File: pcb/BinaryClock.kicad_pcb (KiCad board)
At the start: 2 copper layers, 28.4 x 41.7 mm, 17 parts, among them CON1 AVR-ISP-6, CON2 BARREL_JACK, IC1 ATMEGA328P-A, U1 MC33269, U2 DS3231, U3 clock_header, U4 clock_header, U5 clock_header, Y1 16MHz

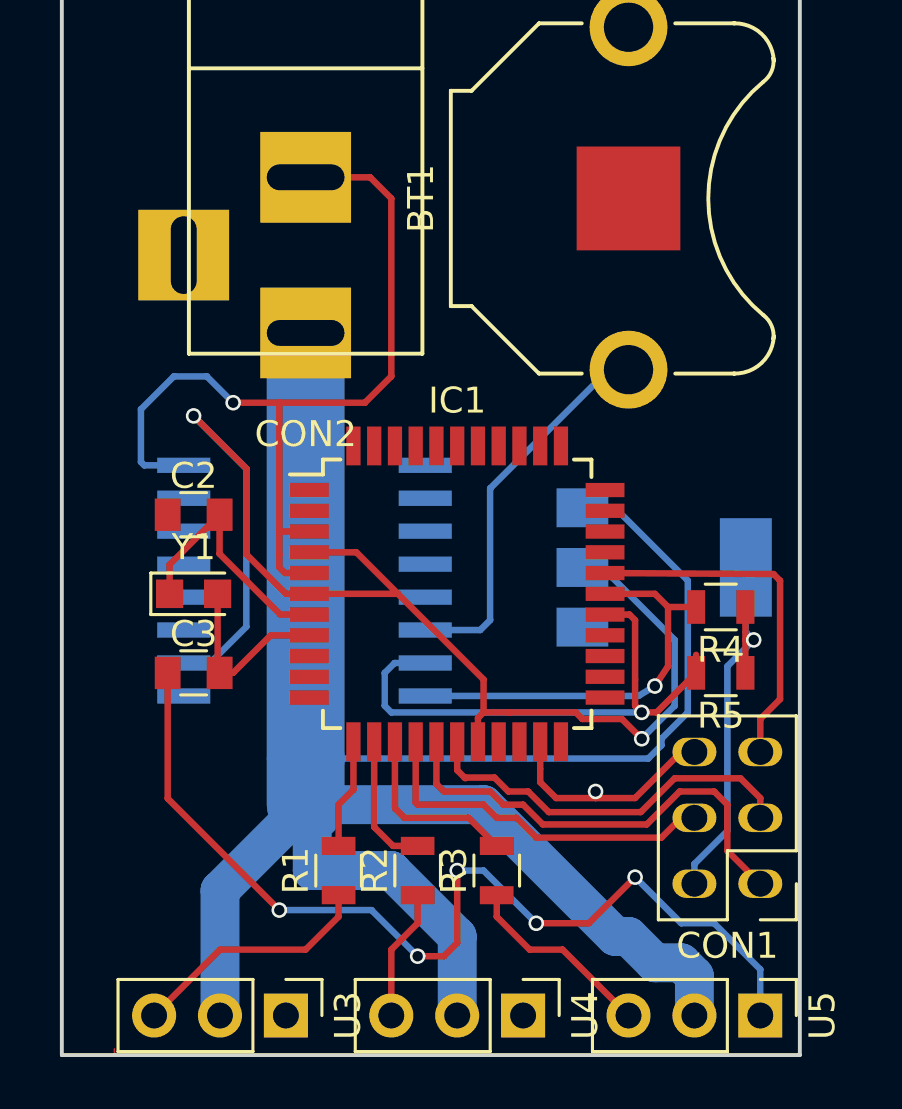
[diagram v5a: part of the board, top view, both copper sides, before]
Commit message: Added silkscreen text
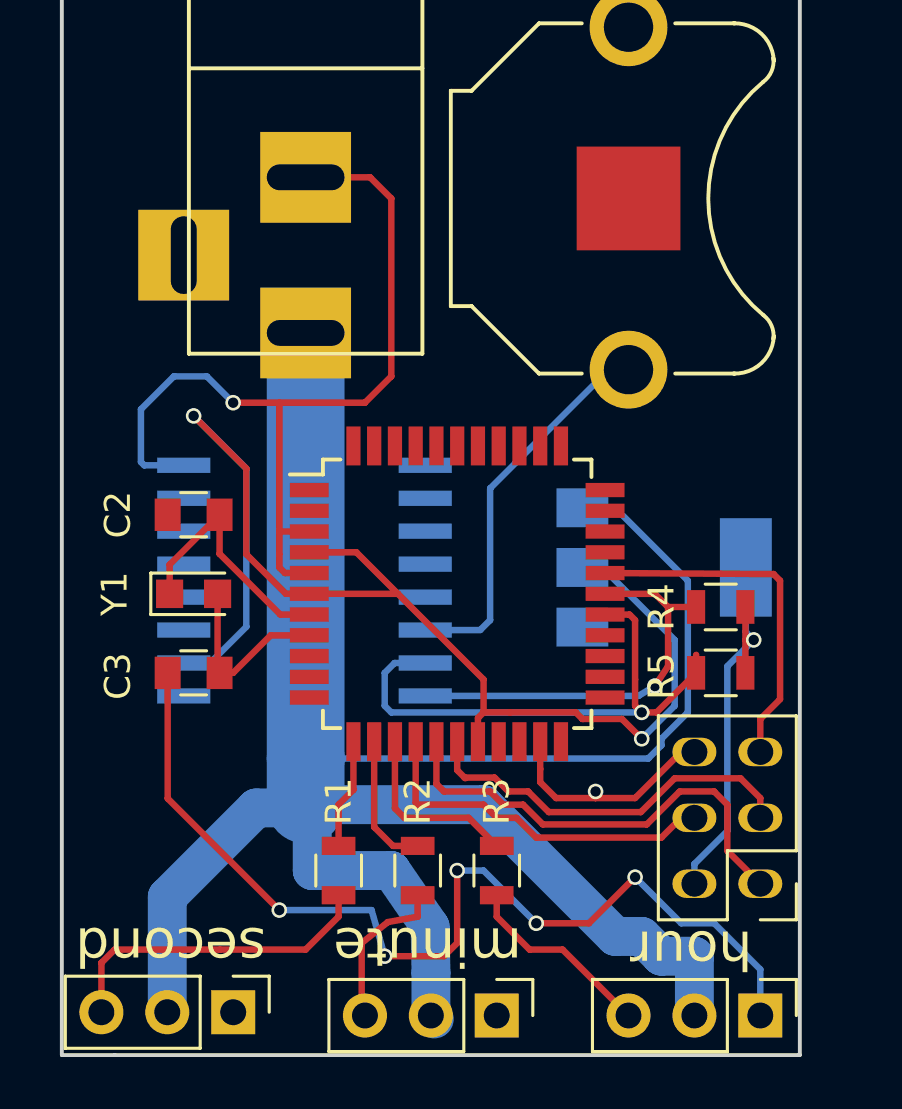
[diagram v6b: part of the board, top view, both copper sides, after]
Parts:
- added G***: LOGO, ais_logo:ais_logo, B.Cu at (163.3, 64.9)
- moved U3 2.04 mm to (150.4, 96.9)
- moved U4 1.02 mm to (160.5, 97.0)
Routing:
- net /LED1: track 9.52 -> 12.6 mm
- net /VIN: track 87.1 -> 89.2 mm
- net /LED2: track 5.06 -> 6.14 mm
- net GND: track 80.7 -> 81.3 mm
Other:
- board text added: "@jinternetthings"
- board text added: "@qnzzo"
- board text added: "Binary Clock v2.0"
- board text added: "Denver, CO"
- board text added: "Made with love at:"
- board text added: "hour"
- board text added: "minute"
- board text added: "second"

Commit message: Removed old bogus atmega328 footprint, replaced with correct TQFP32
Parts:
- removed IC1: ATMEGA328P-A, Housings_QFP:TQFP-44_10x10mm_Pitch0.8mm
- added U6: ATMEGA328-AU, IPC7351-Nominal:QFP80P900X900X120-32, F.Cu at (159.3, 80.3)
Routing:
- net VCC: track 67.5 -> 45.5 mm, vias 3 -> 2
- net /MISO: track 17.8 -> 0.00 mm
- net SCL: track 15.9 -> 0.00 mm, vias 1 -> 0
- net /SCK: track 15.1 -> 0.00 mm
- net /RESET: track 13.8 -> 0.00 mm
- net /MOSI: track 14.0 -> 0.51 mm
- net SDA: track 21.3 -> 13.7 mm, vias 1 -> 0
- net Net-(R3-Pad2): track 7.09 -> 0.00 mm
- net Net-(R2-Pad2): track 5.27 -> 0.00 mm
- net Net-(R1-Pad2): track 4.25 -> 0.00 mm
- net GND: track 81.3 -> 81.4 mm, vias 7 -> 6

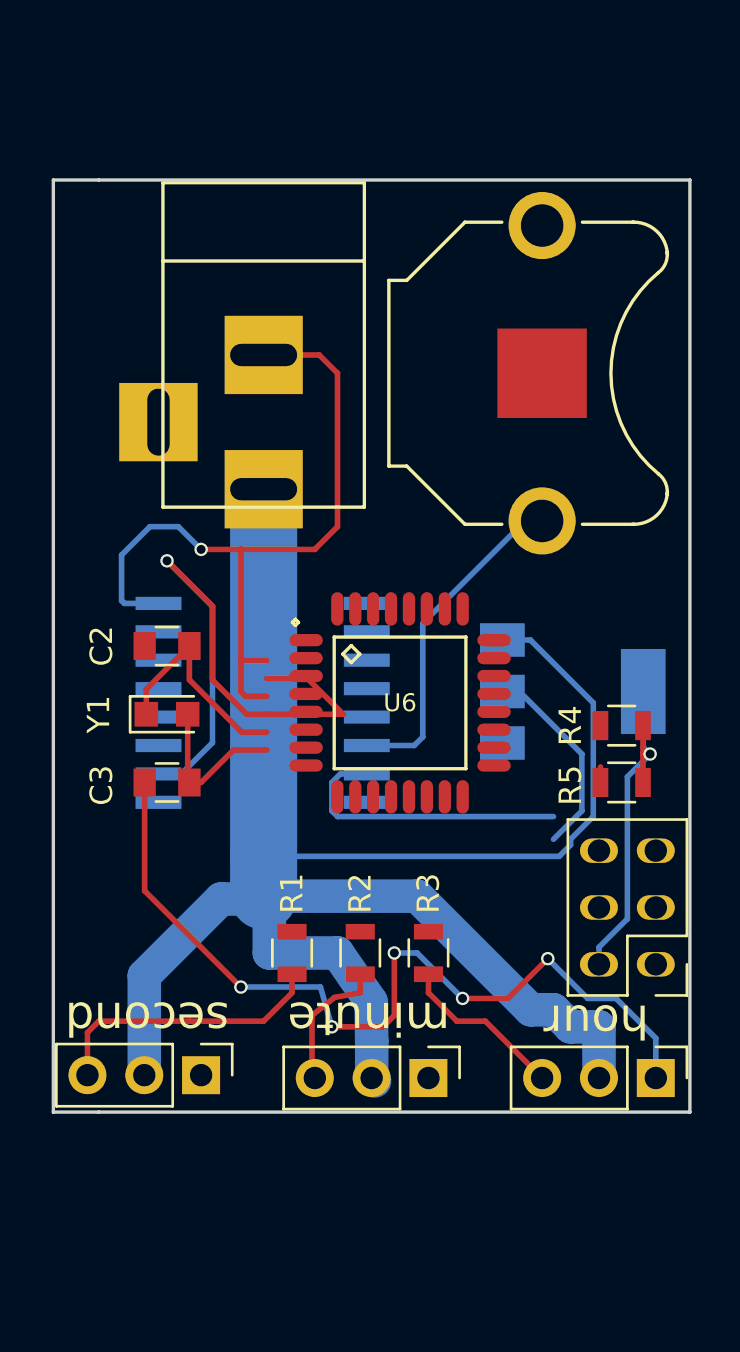
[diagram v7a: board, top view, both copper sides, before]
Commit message: Re-routing with new atmega footprint
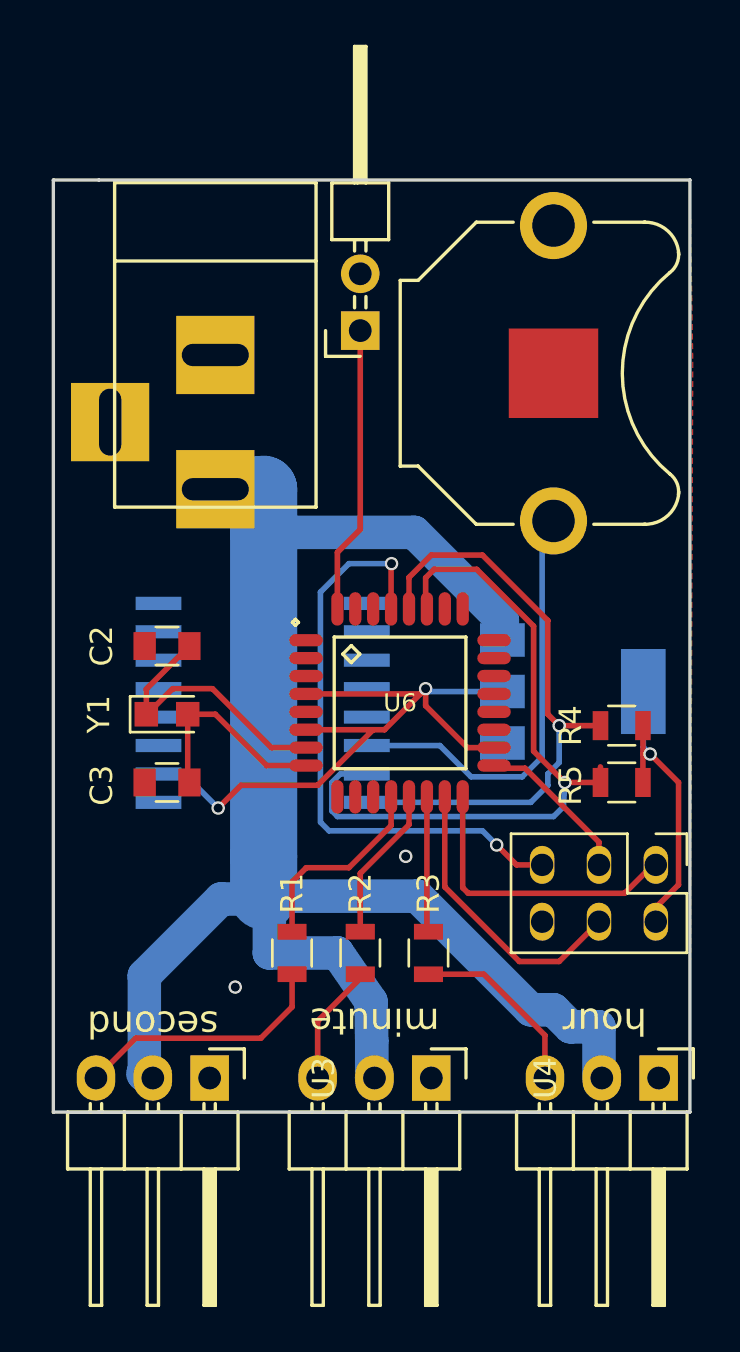
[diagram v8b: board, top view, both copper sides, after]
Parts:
- added ?: SwitchInput, Pin_Headers:Pin_Header_Angled_2x01, F.Cu at (157.5, 63.6)
- ?: renamed from U5; footprint Pin_Headers:Pin_Header_Straight_1x03_Pitch2.54mm -> Pin_Headers:Pin_Header_Angled_1x03
- U3, U4: footprint Pin_Headers:Pin_Header_Straight_1x03_Pitch2.54mm -> Pin_Headers:Pin_Header_Angled_1x03
- moved CON1 4.44 mm to (170.7, 87.5), turned to 270 degrees
- moved CON2 2.16 mm to (151.0, 64.5)
- moved BT1 0.51 mm to (166.1, 65.5)
- moved U3 0.40 mm to (150.7, 97.0)
- moved ? 0.13 mm to (170.8, 97.0)
- moved U4 0.13 mm to (160.7, 97.0)
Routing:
- net GND: track 81.4 -> 0.00 mm, vias 6 -> 0
- net SCL: track 0.00 -> 27.3 mm, vias 0 -> 1
- net /RESET: track 0.00 -> 26.7 mm, vias 0 -> 2
- net SDA: track 13.7 -> 32.2 mm, vias 0 -> 1
- net /MISO: track 0.00 -> 13.7 mm
- net Net-(R7-Pad1): track 0.00 -> 12.9 mm
- net /MOSI: track 0.51 -> 13.0 mm
- net /VIN: track 89.2 -> 78.6 mm
- net Net-(R1-Pad2): track 0.00 -> 8.98 mm
- net /SCK: track 0.00 -> 7.12 mm
- net Net-(R2-Pad2): track 0.00 -> 6.93 mm
- net Net-(R3-Pad2): track 0.00 -> 6.05 mm
- net Net-(BT1-Pad1): track 15.0 -> 19.3 mm
- net Net-(C2-Pad2): track 9.78 -> 12.5 mm
- net Net-(C3-Pad2): track 7.14 -> 9.32 mm
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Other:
- board text added: "Binary Clock v2.1"
- board text removed: "Binary Clock v2.0"
